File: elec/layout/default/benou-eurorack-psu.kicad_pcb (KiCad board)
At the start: 2 copper layers, 225.7 x 100.8 mm, 0 parts

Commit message: init import
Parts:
- added R1: 100.0 Ω, lib:R0402, F.Cu at (250.9, 50.8)
- added U1: , lib:DD-PAK-5_L10.2-W8.9-P1.70-LS14.0-BR, F.Cu at (239.7, 42.0)
- added U2: ?, Package_TO_SOT_SMD:TO-263-2, F.Cu at (240.5, 56.0)

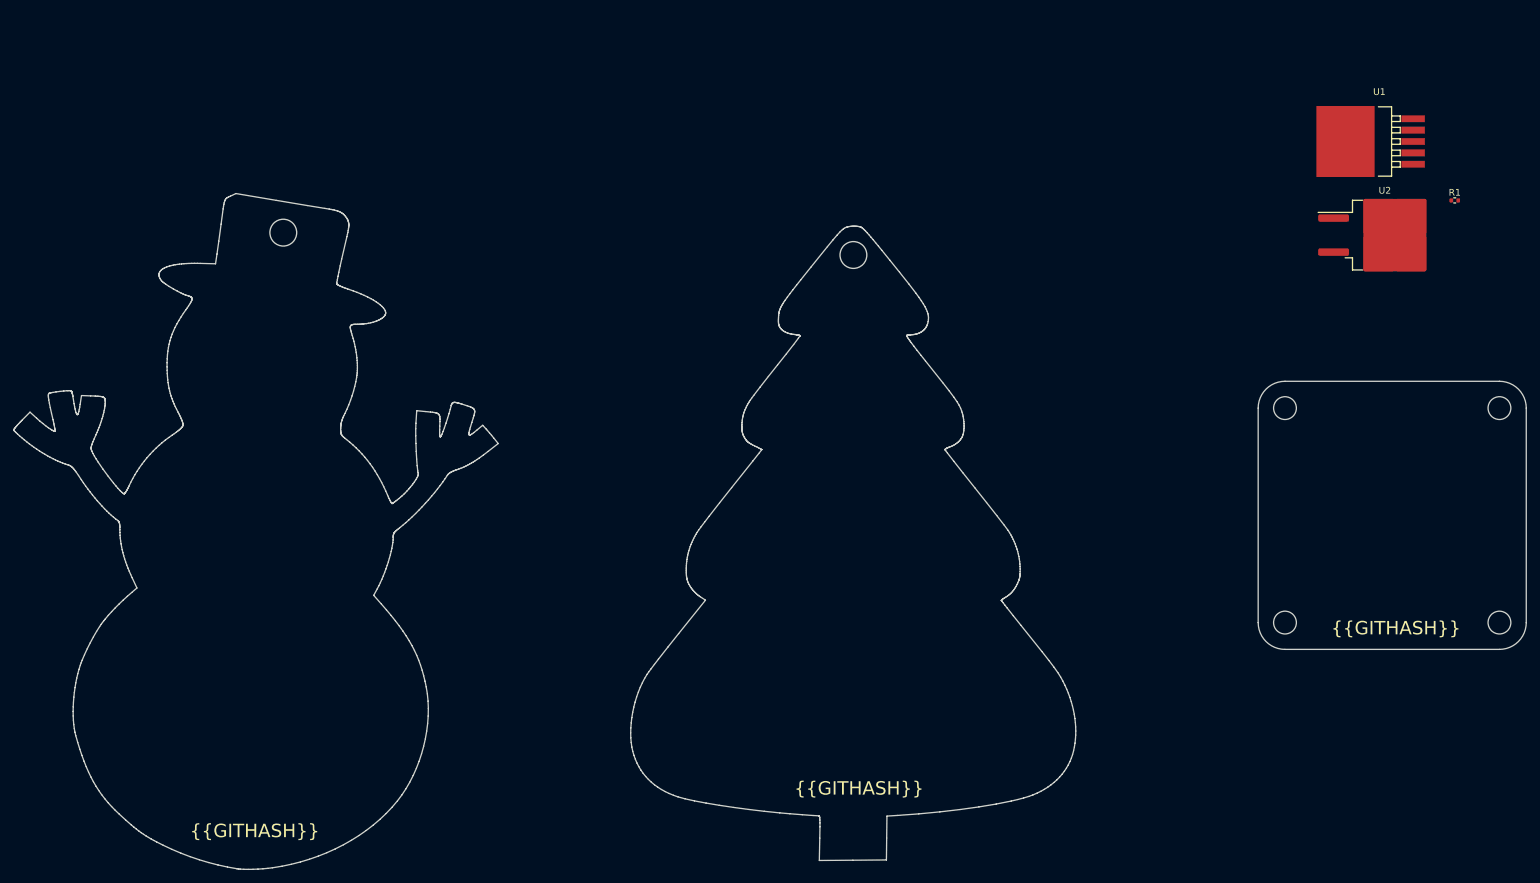
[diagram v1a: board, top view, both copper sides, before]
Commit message: add IRM footprint
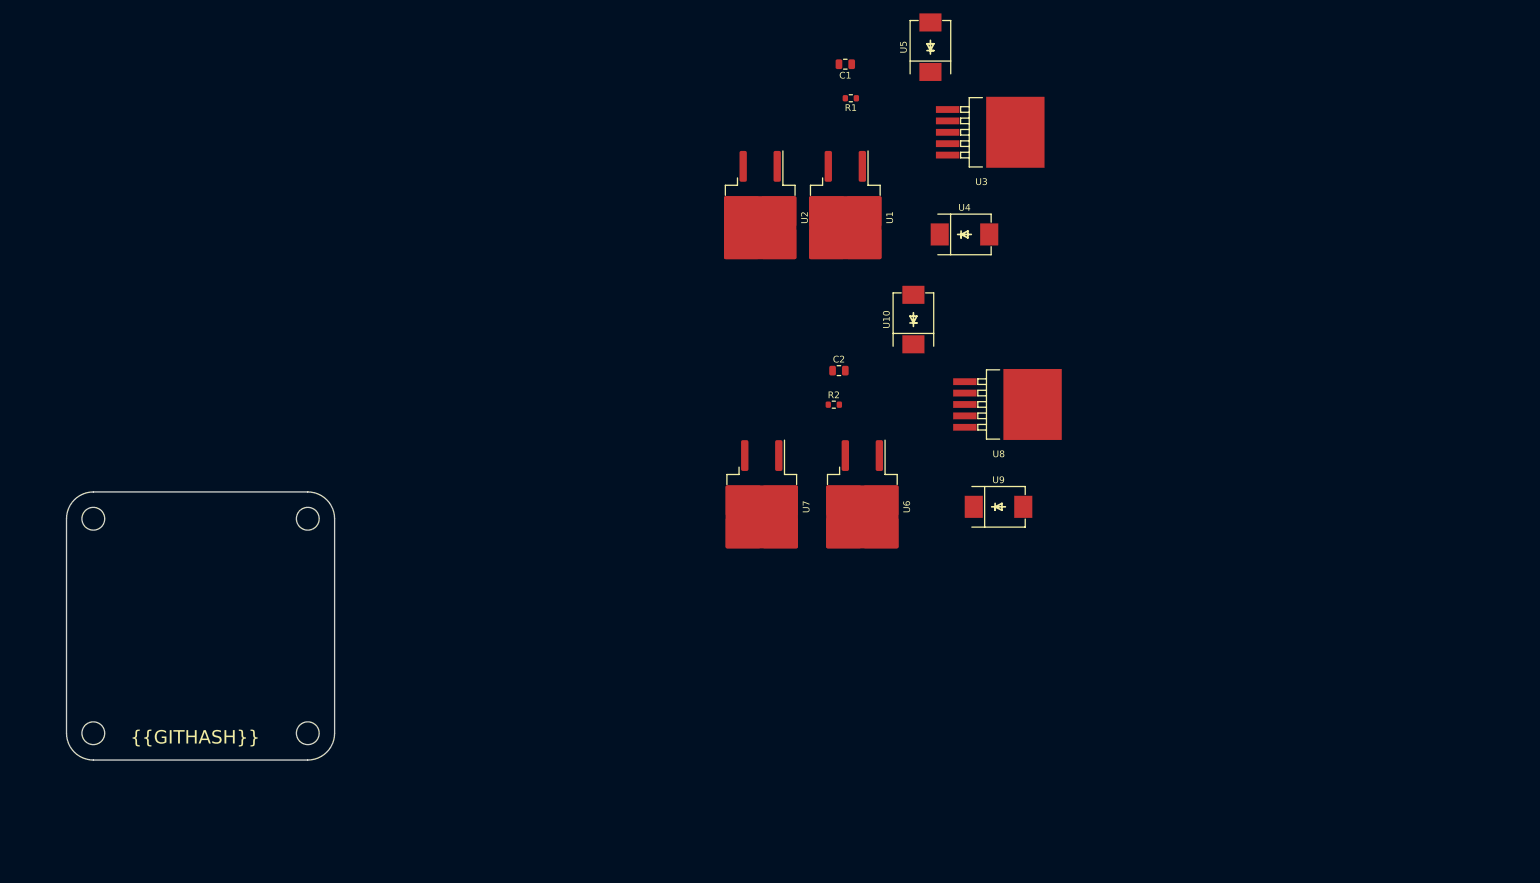
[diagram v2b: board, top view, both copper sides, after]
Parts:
- added C1: 10.0 pF, lib:C0805, F.Cu at (160.0, 30.5)
- added C2: 10.0 pF, lib:C0805, F.Cu at (159.1, 76.2)
- added R2: 220.0 KΩ, lib:R0603, F.Cu at (158.3, 81.3)
- added U10: , lib:SMC_L6.9-W5.9-LS7.9-RD, F.Cu at (170.2, 68.6)
- added U3: , lib:DD-PAK-5_L10.2-W8.9-P1.70-LS14.0-BR, F.Cu at (180.3, 40.6)
- added U4: , lib:SMC_L6.9-W5.9-LS7.9-RD, F.Cu at (177.8, 55.9)
- added U5: , lib:SMC_L6.9-W5.9-LS7.9-RD, F.Cu at (172.7, 27.9)
- added U6: ?, Package_TO_SOT_SMD:TO-263-2, F.Cu at (162.6, 96.5)
- added U7: ?, Package_TO_SOT_SMD:TO-263-2, F.Cu at (147.6, 96.5)
- added U8: , lib:DD-PAK-5_L10.2-W8.9-P1.70-LS14.0-BR, F.Cu at (182.9, 81.2)
- added U9: , lib:SMC_L6.9-W5.9-LS7.9-RD, F.Cu at (182.9, 96.5)
- R1: value 100.0 Ω -> 220.0 KΩ; footprint lib:R0402 -> lib:R0603
- U1: value (none) -> ?; footprint lib:DD-PAK-5_L10.2-W8.9-P1.70-LS14.0-BR -> Package_TO_SOT_SMD:TO-263-2
- moved U2 93.2 mm to (147.3, 53.4), turned to -90 degrees
- moved R1 91.4 mm to (160.8, 35.6), turned to 180 degrees
- moved U1 80.5 mm to (160.0, 53.4), turned to -90 degrees
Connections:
- R1 pad 1: vcc -> p1
- R1 pad 2: gnd -> voltage_negative
- U1 pad 1: NC -> voltage_positive
- U1 pad 2: SET -> sink
- U1 pad 3: OUT -> p2
- U2 pad 1: p1 -> p2
- U2 pad 2: sink -> sink-1
- U2 pad 3: p2 -> p2-1
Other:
- board size 225.7 x 100.8 mm -> 40 x 40 mm

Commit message: add footprints and init board layout
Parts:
- added C3: 10.0 pF, lib:C0805, F.Cu at (168.5, 121.3)
- added R3: 100k, lib:R1210, F.Cu at (168.7, 114.3)
- added U11: ?, Package_TO_SOT_SMD:TO-263-2, F.Cu at (167.9, 140.6)
- added U12: ?, Package_TO_SOT_SMD:TO-263-2, F.Cu at (152.4, 139.7)
- added U13: , lib:DD-PAK-5_L10.2-W8.9-P1.70-LS14.0-BR, F.Cu at (185.4, 124.5)
- added U14: , lib:SMC_L6.9-W5.9-LS7.9-RD, F.Cu at (180.3, 111.8)
- added U15: , lib:SMC_L6.9-W5.9-LS7.9-RD, F.Cu at (185.4, 137.2)
- added U16: ?, lib:IRM-30-15, F.Cu at (91.2, 44.1)
- added U17: ?, lib:IRM-30-15, F.Cu at (91.2, 86.7)
- added U18: ?, lib:PSK-30D-9, F.Cu at (91.4, 134.6)
- R1, R2: value 220.0 KΩ -> 240k; footprint lib:R0603 -> lib:R1210
- moved U6 25.5 mm to (137.2, 94.0), turned to 90 degrees
- moved U7 10.3 mm to (157.5, 94.0), turned to 90 degrees
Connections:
- U1 pad 1: voltage_positive -> voltage_positive-2
- U3 pad 4: voltage_positive -> voltage_positive-2
- U6 pad 1: voltage_positive-2 -> voltage_positive-3
- U8 pad 4: voltage_positive-2 -> voltage_positive-3
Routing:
- net L: track 0.00 -> 149.4 mm
- net N: track 0.00 -> 118.7 mm
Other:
- board size 40 x 40 mm -> 172.7 x 142.2 mm

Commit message: make netlist ready for layout
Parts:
- added U19: , lib:CONN-TH_63849-1, F.Cu at (43.2, 58.4)
- added U20: , lib:CONN-TH_63849-1, F.Cu at (38.1, 81.3)
- added U21: , lib:CONN-TH_63849-1, F.Cu at (40.7, 25.4)
- added U22: , lib:CONN-TH_T34001, F.Cu at (223.6, 34.5)
- added U23: , lib:CONN-TH_T34001, F.Cu at (221.0, 69.6)
- added U24: , lib:CONN-TH_T34001, F.Cu at (221.0, 133.6)
- added U25: , lib:CONN-TH_T34001, F.Cu at (221.0, 95.5)
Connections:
- net OUT renamed voltage_positive
- net OUT-2 renamed voltage_positive-1
- U10 pad 1: OUT-1 -> voltage_negative
- U8 pad 3: OUT-1 -> voltage_negative
- U8 pad 6: OUT-1 -> voltage_negative
- U9 pad 2: OUT-1 -> voltage_negative
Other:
- board size 172.7 x 142.2 mm -> 210.8 x 142.2 mm

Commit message: move floating LDO to a dedicated module
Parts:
- moved C2 73.0 mm to (207.1, 21.2)
- moved C3 73.0 mm to (216.5, 66.3)
- moved R1 73.0 mm to (208.9, -19.4)
- moved R2 73.0 mm to (206.3, 26.3)
- moved R3 73.0 mm to (216.7, 59.3)
- moved U10 73.0 mm to (218.2, 13.6)
- moved U13 73.0 mm to (233.4, 69.5)
- moved U14 73.0 mm to (228.4, 56.8)
- moved U15 73.0 mm to (233.4, 82.2)
- moved U2 73.0 mm to (195.3, -1.61)
- moved U23 73.0 mm to (269.0, 14.7)
- moved U24 73.0 mm to (269.0, 78.6)
- moved U3 73.0 mm to (228.4, -14.3)
- moved U5 73.0 mm to (220.7, -27.0)
- moved U6 73.0 mm to (185.2, 39.0)
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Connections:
- net voltage_negative renamed v_neg
- net voltage_negative-1 renamed v_neg-1
- net voltage_positive renamed v_pos
- net voltage_positive-1 renamed v_pos-1
- net voltage_positive-2 renamed v_pos-2
- net voltage_positive-3 renamed v_pos-3
- net voltage_positive-4 renamed v_pos-4
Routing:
- net L: track 149.4 -> 0.00 mm
- net N: track 118.7 -> 0.00 mm

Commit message: finish first rev layout
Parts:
- added BenouGraphic: , benou:Benou_bot_graphics_15mm, B.Cu at (116.0, 141.0)
- added C2: 22uF, lib:C1206, F.Cu at (181.0, 69.0)
- added C3: 22uF, lib:C1206, F.Cu at (207.5, 52.0)
- added C5: 22uF, lib:C1206, F.Cu at (180.5, 101.0)
- added C6: 22uF, lib:C1206, F.Cu at (207.5, 83.5)
- added C8: 22uF, lib:C1206, F.Cu at (179.0, 129.5)
- added C9: 22uF, lib:C1206, F.Cu at (208.1, 114.0)
- R1, R2: value 240k -> 243k; footprint lib:R1210 -> lib:R0805
- R3: footprint lib:R1210 -> lib:R0805
- moved U22 83.1 mm to (241.5, 57.0)
- moved U5 78.5 mm to (199.5, 48.5), turned to 0 degrees
- moved C1 75.8 mm to (214.0, 51.0), turned to 90 degrees
- moved U14 70.6 mm to (221.3, 127.0)
- moved R1 70.5 mm to (211.5, 51.0), turned to 90 degrees
- moved U10 69.0 mm to (199.5, 80.0), turned to 0 degrees
- moved U3 68.6 mm to (223.0, 54.0)
- moved U23 68.4 mm to (241.0, 77.0)
- moved U1 66.6 mm to (189.5, 62.4), turned to 90 degrees
- moved U25 65.0 mm to (243.0, 100.0)
- moved U4 64.3 mm to (221.5, 65.0)
- moved U2 64.2 mm to (203.0, 62.1), turned to 90 degrees
- moved C4 61.2 mm to (214.0, 82.0), turned to 90 degrees
- moved U8 59.3 mm to (223.0, 85.0)
- moved R2 55.9 mm to (211.5, 82.0), turned to 90 degrees
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- renumbered C2 to C4, C3 to C7
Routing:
- net v_pos-3: track 0.00 -> 49.1 mm, vias 0 -> 2
- net v_pos-4: track 0.00 -> 48.7 mm, vias 0 -> 2
- net v_pos-2: track 0.00 -> 48.3 mm, vias 0 -> 2
- net p1-1: track 0.00 -> 6.61 mm
- net p1: track 0.00 -> 6.61 mm
- net p1-2: track 0.00 -> 6.52 mm
- net v_neg: vias 0 -> 8
- added copper zone on F.Cu, net L
- added copper zone on F.Cu, net N
- added copper zone on F.Cu, net p2
- added copper zone on F.Cu, net p2-1
- added copper zone on F.Cu, net p2-2
- added copper zone on F.Cu, net p2-3
- added copper zone on F.Cu, net p2-4
- added copper zone on F.Cu, net p2-5
- added copper zone on B.Cu, net v_neg
- added copper zone on F.Cu, net v_neg
- added copper zone on F.Cu, net v_neg-1
- added copper zone on F.Cu, net v_pos
- added copper zone on F.Cu, net v_pos-1
- added copper zone on F.Cu, net v_pos-2
- added copper zone on F.Cu, net v_pos-3
- added copper zone on F.Cu, net v_pos-4
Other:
- board size 210.8 x 142.2 mm -> 200 x 120 mm
- board text added: "Eurorack power supply made with .atopile"

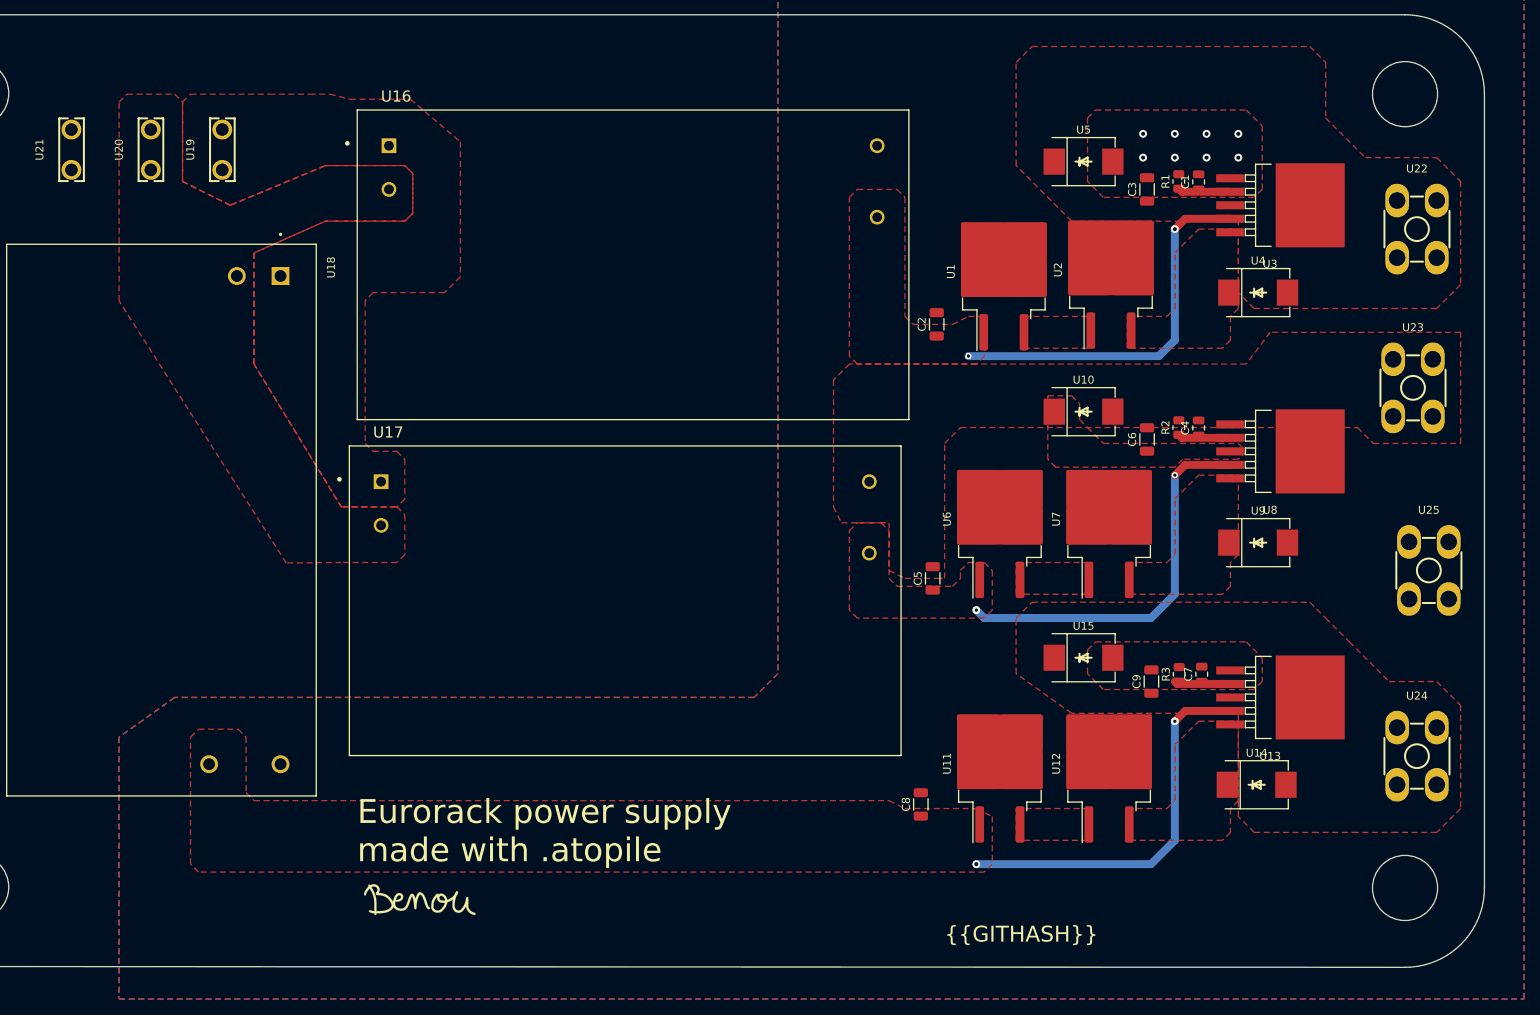
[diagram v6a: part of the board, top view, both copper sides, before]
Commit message: improve layout's thermal dissipation
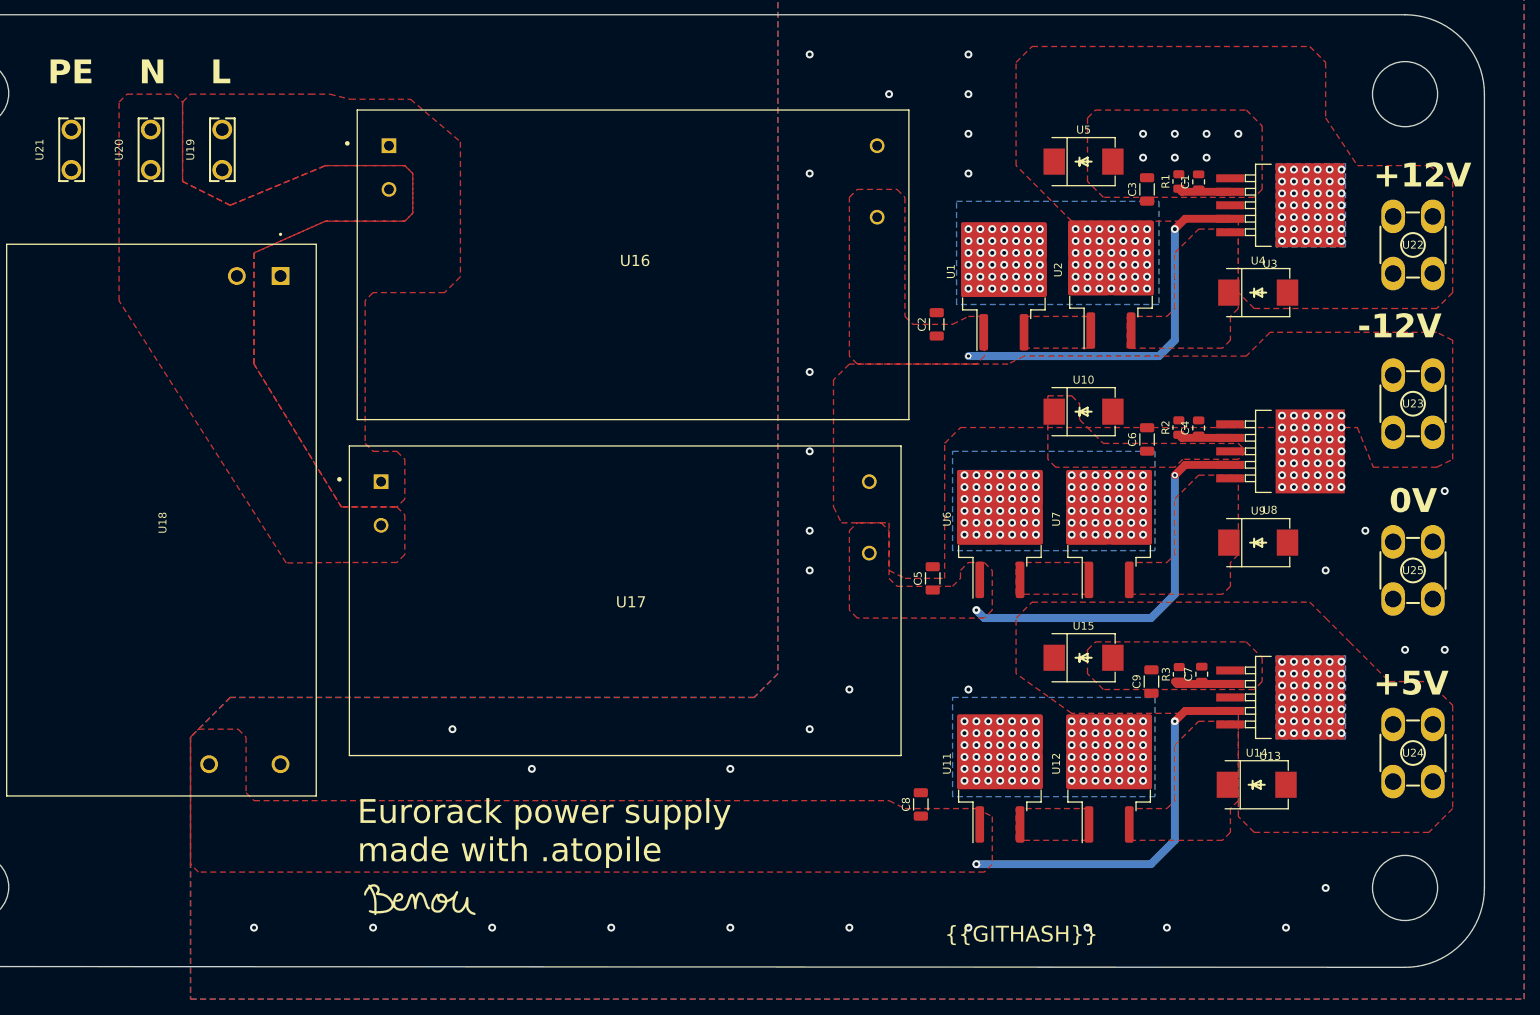
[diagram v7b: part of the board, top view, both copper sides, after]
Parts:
- moved U22 2.06 mm to (241.0, 59.0)
- moved U23 2.00 mm to (241.0, 79.0)
- moved U25 2.00 mm to (241.0, 100.0)
- moved U24 0.64 mm to (241.0, 123.0)
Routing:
- net v_pos-1: vias 0 -> 42
- net v_pos: vias 0 -> 42
- net v_neg: vias 8 -> 82
- net sink-5: vias 0 -> 42
- net sink-4: vias 0 -> 42
- net sink-3: vias 0 -> 42
- net sink-2: vias 0 -> 42
- net sink-1: vias 0 -> 42
- net sink: vias 0 -> 42
- added copper zone on B.Cu, net (none)
- added copper zone on B.Cu, net v_pos
- added copper zone on B.Cu, net v_pos-1
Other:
- board text added: "+12V"
- board text added: "+5V"
- board text added: "-12V"
- board text added: "0V"
- board text added: "L"
- board text added: "N"
- board text added: "PE"
- board text added: "U11"
